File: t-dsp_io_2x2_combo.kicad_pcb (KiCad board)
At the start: 2 copper layers, 100 x 50 mm, 12 parts, among them J1 XLRM_NC3MAH, J10 COMBO_NCJ6FA-H, J11 B2B-XH-A, J2 XLRM_NC3MAH, J6 Conn_02x03_Odd_Even, J7 Conn_02x03_Odd_Even, J8 B2B-XH-A, J9 COMBO_NCJ6FA-H

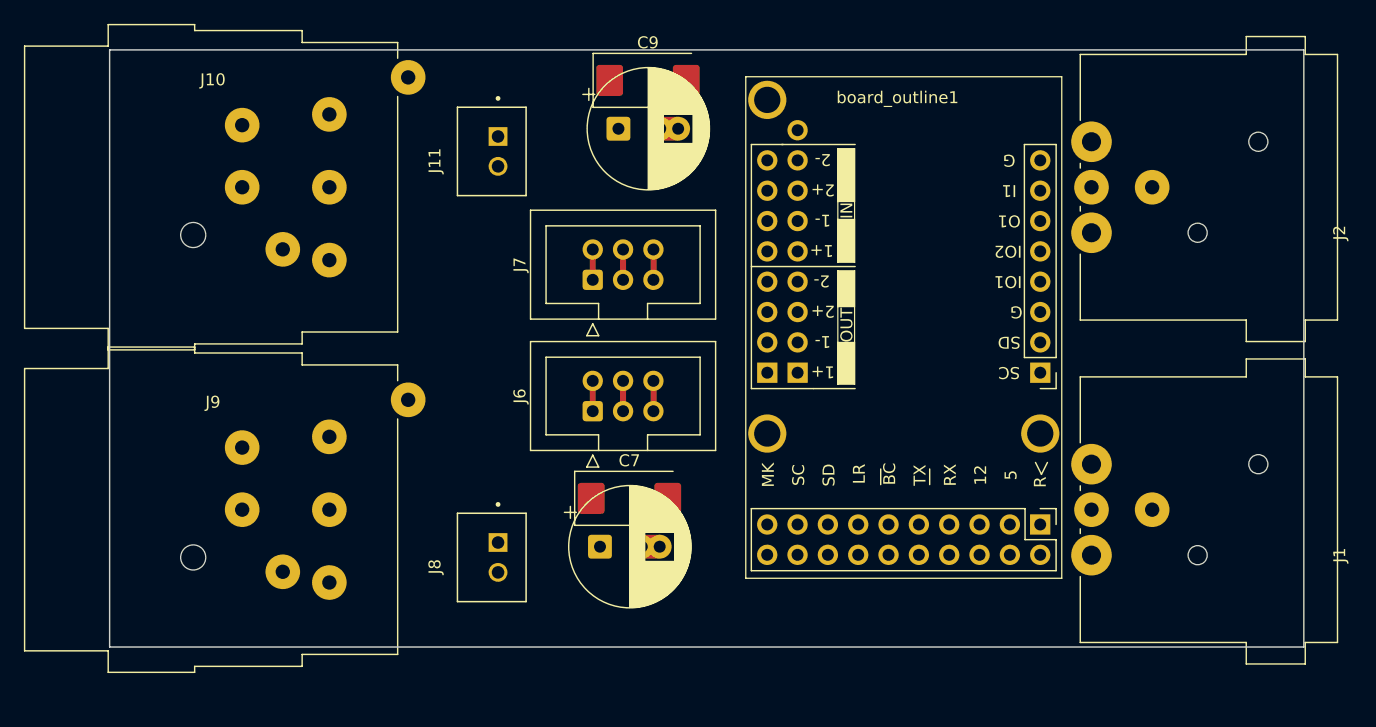
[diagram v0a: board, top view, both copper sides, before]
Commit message: Rename to t-dsp_io_2x2_combo and prepare for public release
- Rename project files from t-dsp_dual_preamp to t-dsp_io_2x2_combo
- Add README, LICENSE (CC BY-NC-SA 4.0), schematic PDF, interactive BOM
- Add 3D render images for documentation
- Remove third-party datasheets (docs/), old revisions, downloaded library ZIPs
- Update .gitignore for clean repo
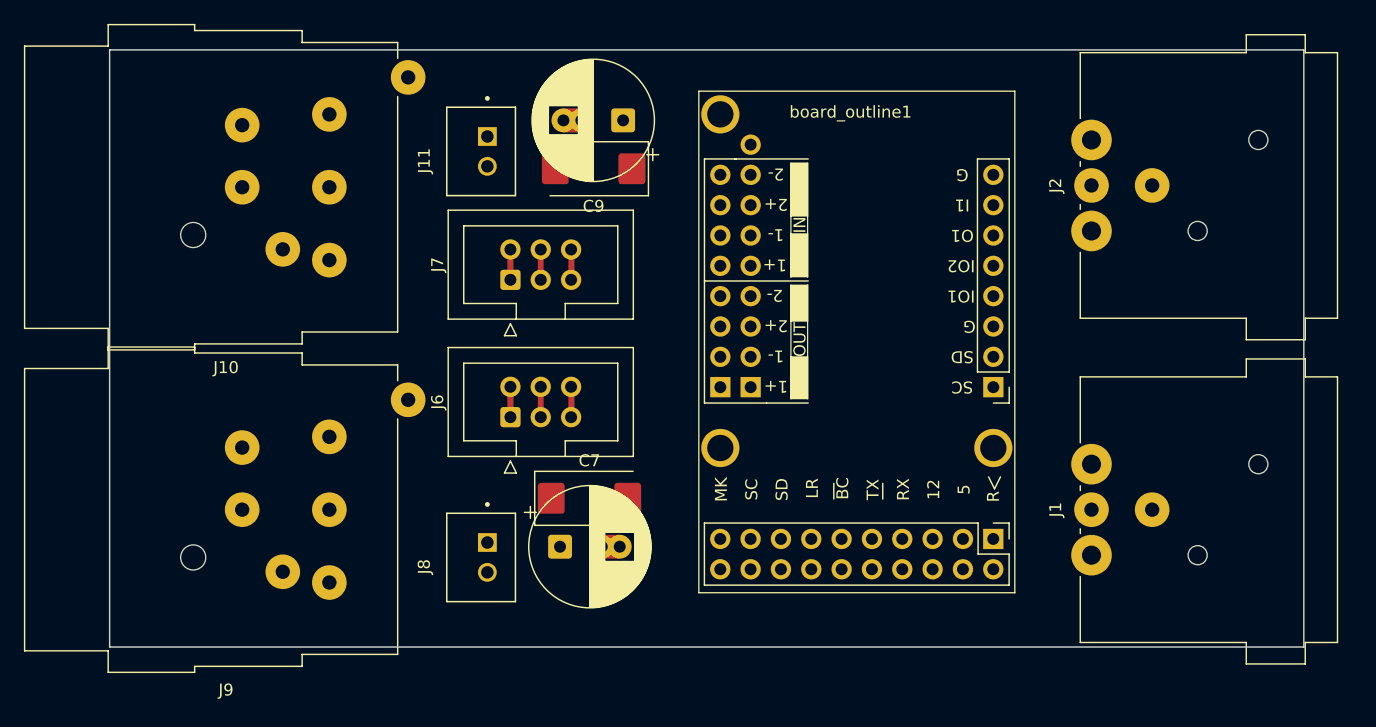
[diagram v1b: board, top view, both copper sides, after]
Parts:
- J1, J2: value XLRM_NC3MAH -> XLR3_Ground
- moved J6 6.91 mm to (133.6, 80.8)
- moved J7 6.89 mm to (133.6, 69.3)
- moved board_outline1 4.11 mm to (175.8, 95.5)
- moved C7 3.35 mm to (137.7, 91.6)
- moved J11 0.89 mm to (131.1, 58.5)
- moved J8 0.89 mm to (131.1, 92.5)
- moved C9 0.80 mm to (143.0, 55.9), turned to 180 degrees
- moved J2 0.15 mm to (200.0, 61.4)
